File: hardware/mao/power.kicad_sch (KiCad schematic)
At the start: 36 parts, among them J101 USB-C, J102 BAT, Q101 AO3401A, U101 TPD2E2U06, U102 BQ24073RGTR, U103 MAX17048G+T10, U104 TPS63802DLAR, U105 TPS22919DCKR

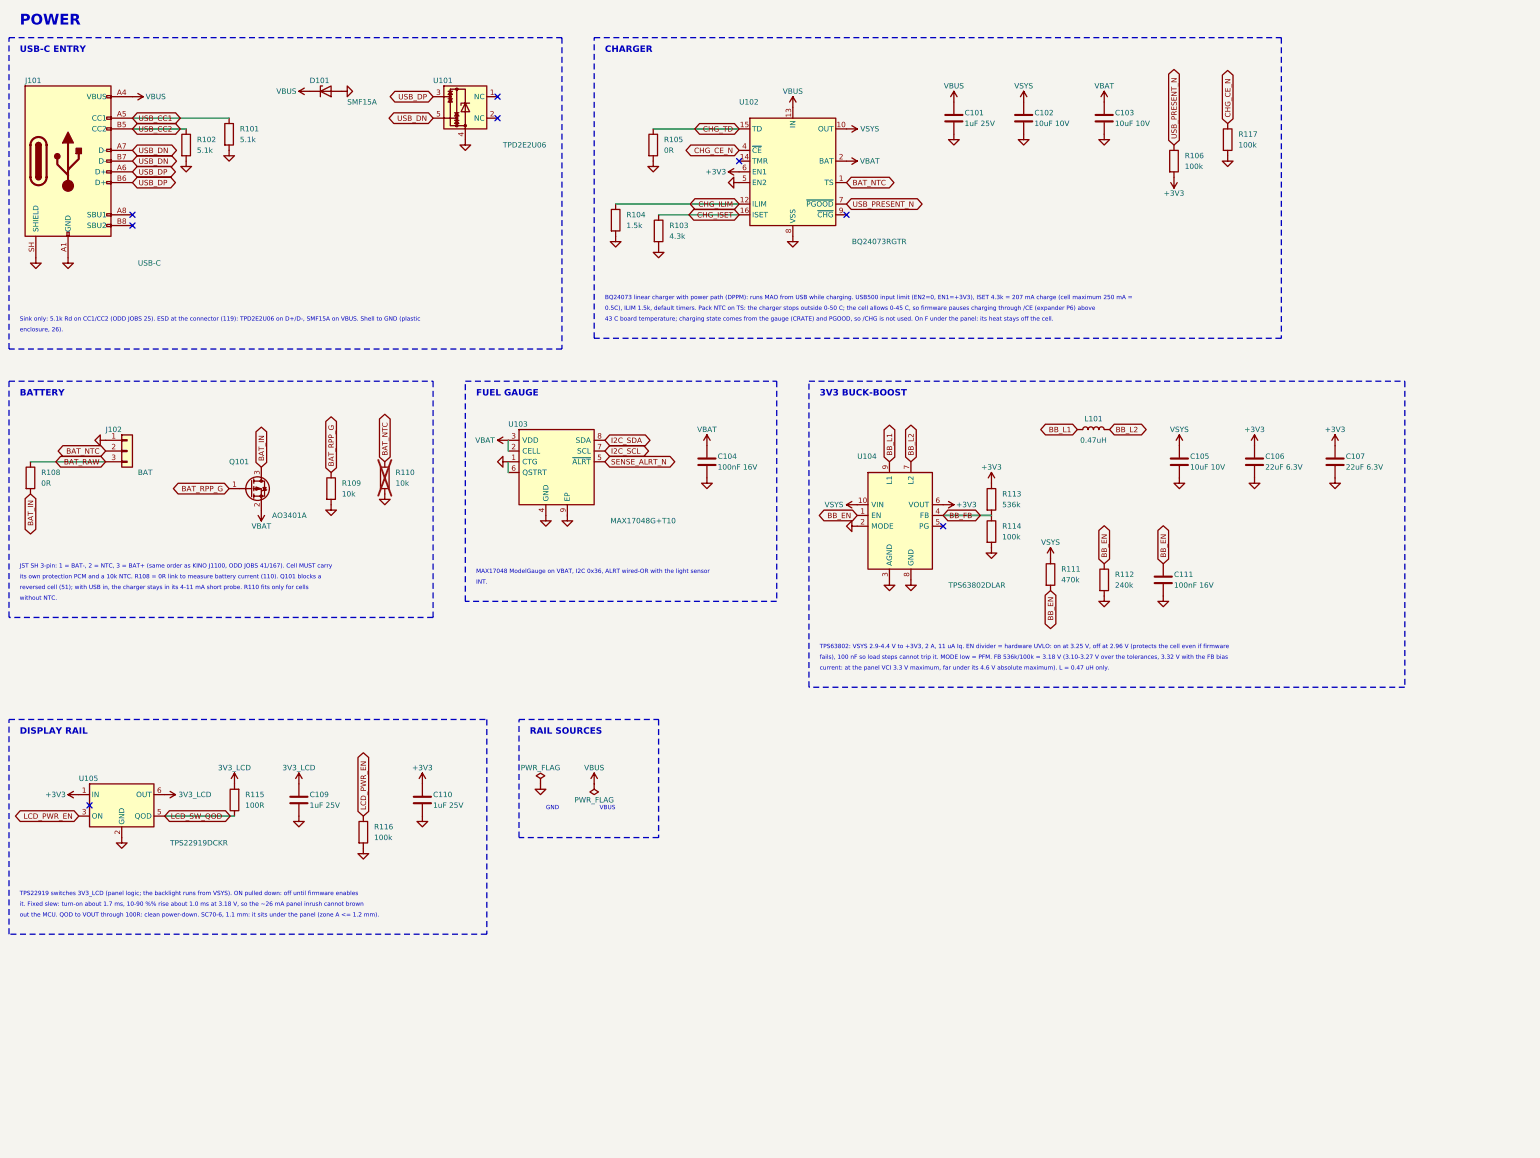
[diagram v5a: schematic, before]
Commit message: A1 capture: Gate C architecture on the A0 puck (schematic, ERC 0)
circuit.py now describes MAO_MAIN A1 (ERC 0 at all severities, 137 parts, 75 nets):
- ESP32-S3-MINI-1-N8 on RF_Module:ESP32-S2-MINI-1 (Gate C land audit); GPIO0 = BOOT pad only
  (10k + TP8), GPIO3/45/46 NC, 22R + DNP 10 pF on USB at the module, VBUS_SENSE 100k/150k.
- BQ25185 (ILIM/VSET 18k: 4.2 V / 500 mA; ISET 1.43k: 210 mA as A0; TS/MR to the NTC, DNP 10k,
  TSMR pad; /CE 100k pull-down; STAT1/2 10k to +3V3) replaces BQ24073.
- TPS62840 (VSET 102k = 3.2 V, SLVSEC6D table 1; 2.2 uH, CIN 4.7 uF, COUT 10 uF; MODE/STOP low,
  EN to VIN) replaces TPS63802 and its UVLO/FB dividers; LINK_REG 0R added, LINK_BAT kept.
- ICM-42670-P replaces LSM6DSOX on the same land (0x68, INT1 100k pull-up, INT2 not wired).
- DRV2605L VDD and pin 6 on +3V3; constant-current backlight sink (TLV9061 + DMG2302UK, 3.3R)
  replaces the AW9364; TPS22916C for the panel rail and the IR receiver rail.
- MAX98357A SD_MODE straight from GPIO9 (2.2k series dropped: +3V3 <= VSYS by topology).
- Removed: touch (4 zones, electrodes, springs), SPH0641, OPT3004, TCA6408A, board-ID divider.
- I2C pull-ups 4.7k; new fixture pads BL, AMP, TE, PRS, HLA, TSMR, CE, IO21, IO26.
- Battery connector stays JST SH: the Gate C JST PH side entry is 4.8 mm tall (KiCad STEP of the
  PH side-entry housing) against the 3.2 mm B-side zone over the cell; owner decision.
Parts kept from A0 keep their references; removed numbers are retired.
New footprint MAO:TI_DLC0008B_VSON-HR-8 (TI land example 4224310/A, from the Gate C generator);
A0-only custom footprints removed. Board name MAO_MAIN_A1; A0 board/outputs removed from this tree
(they stay on the A0 branch).

Co-Authored-By: Claude Opus 5.5 <noreply@anthropic.com>
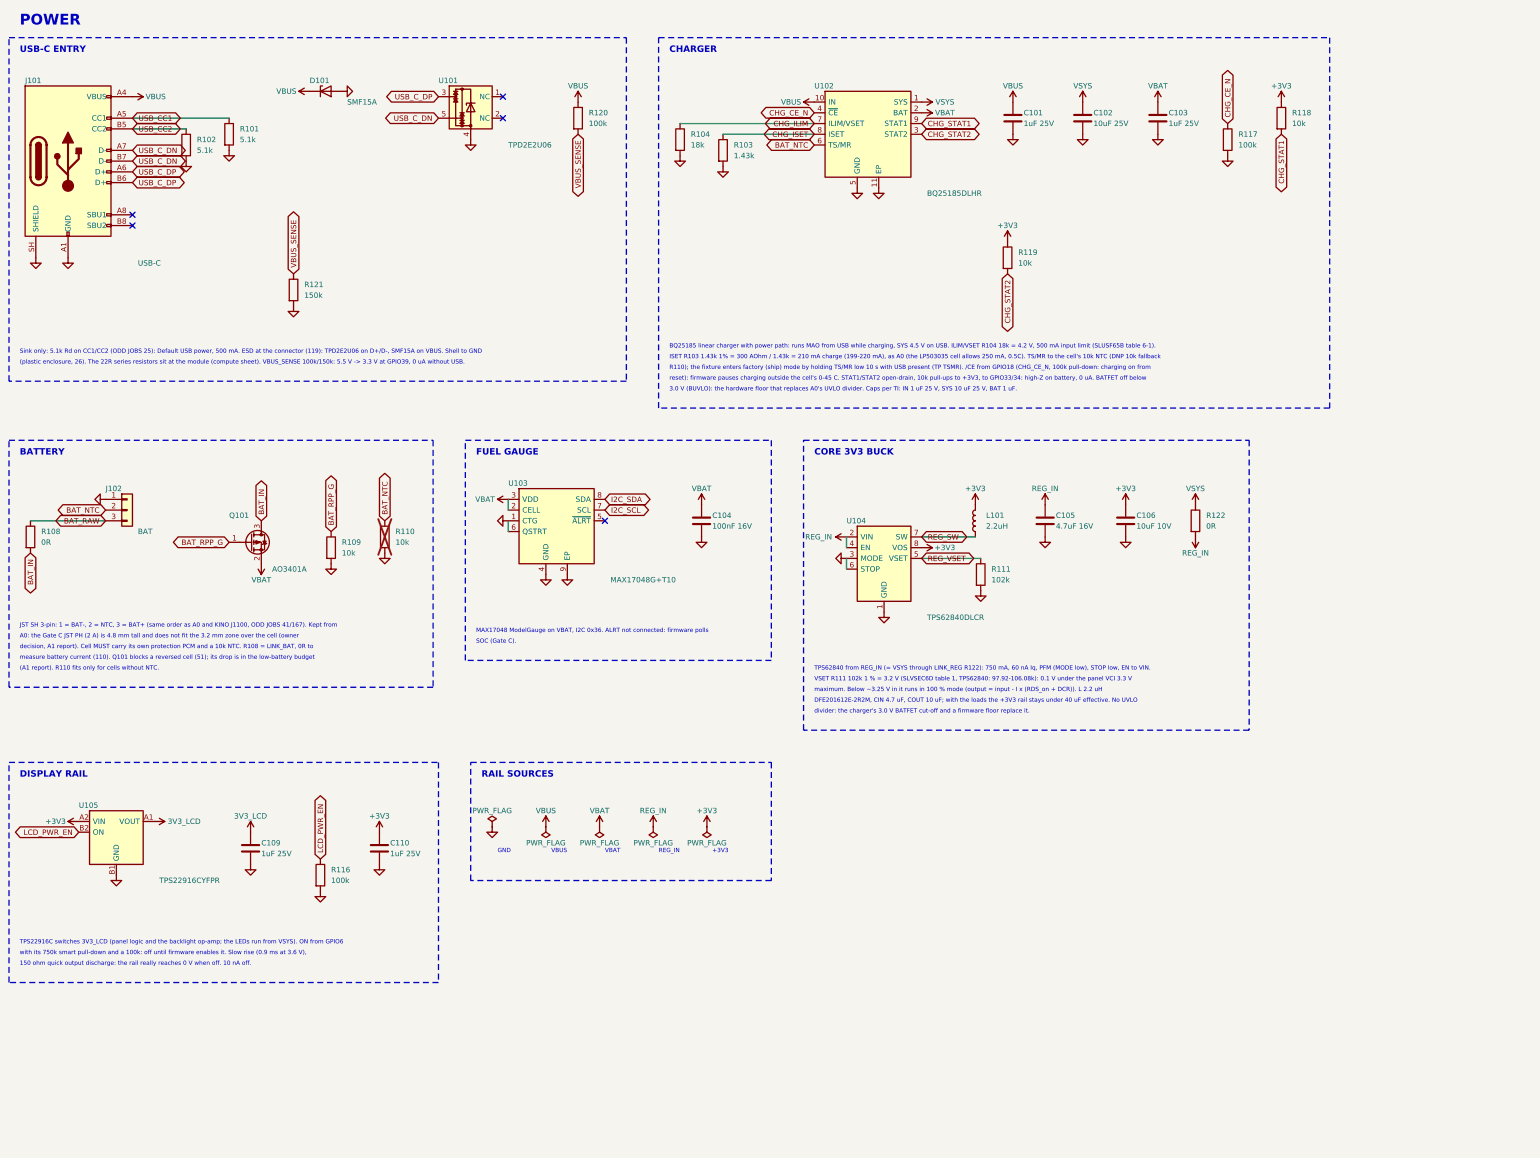
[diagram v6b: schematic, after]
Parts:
- removed C107: 22uF 6.3V, Capacitor_SMD:C_0603_1608Metric, symbol Device:C
- removed C111: 100nF 16V, Capacitor_SMD:C_0402_1005Metric, symbol Device:C
- removed R105: 0R, Resistor_SMD:R_0402_1005Metric, symbol Device:R
- removed R106, R114: 100k, Resistor_SMD:R_0402_1005Metric, symbol Device:R
- removed R112: 240k, Resistor_SMD:R_0402_1005Metric, symbol Device:R
- removed R113: 536k, Resistor_SMD:R_0402_1005Metric, symbol Device:R
- removed R115: 100R, Resistor_SMD:R_0402_1005Metric, symbol Device:R
- added R118, R119: 10k, Resistor_SMD:R_0402_1005Metric, symbol Device:R
- added R120: 100k, Resistor_SMD:R_0402_1005Metric, symbol Device:R
- added R121: 150k, Resistor_SMD:R_0402_1005Metric, symbol Device:R
- added R122: 0R, Resistor_SMD:R_0603_1608Metric, symbol Device:R
- C102: value 10uF 10V -> 10uF 25V; LCSC C19702 -> C96446; MPN CL10A106KP8NNNC -> CL10A106MA8NRNC
- C103: value 10uF 10V -> 1uF 25V; footprint Capacitor_SMD:C_0603_1608Metric -> Capacitor_SMD:C_0402_1005Metric; LCSC C19702 -> C52923; MPN CL10A106KP8NNNC -> CL05A105KA5NQNC
- C105: value 10uF 10V -> 4.7uF 16V; LCSC C19702 -> C19666; MPN CL10A106KP8NNNC -> CL10A475KO8NNNC
- C106: value 22uF 6.3V -> 10uF 10V; LCSC C59461 -> C19702; MPN CL10A226MQ8NRNC -> CL10A106KP8NNNC
- L101: value 0.47uH -> 2.2uH; LCSC C668312 -> C337893; MPN DFE201612E-R47M=P2 -> DFE201612E-2R2M=P2
- R103: value 4.3k -> 1.43k; LCSC C25899 -> C163483; MPN 0402WGF4301TCE -> RC0402FR-071K43L; Manufacturer UNI-ROYAL -> YAGEO
- R104: value 1.5k -> 18k; LCSC C25867 -> C25762; MPN 0402WGF1501TCE -> 0402WGF1802TCE
- R111: value 470k -> 102k; LCSC C25790 -> C2933066; MPN 0402WGF4703TCE -> FRC0402F1023TS; Manufacturer UNI-ROYAL -> FOJAN
- U102: value BQ24073RGTR -> BQ25185DLHR; footprint Package_DFN_QFN:VQFN-16-1EP_3x3mm_P0.5mm_EP1.68x1.68mm_ThermalVias -> Package_DFN_QFN:Texas_DLH0010A_WSON-10-1EP_2.2x2mm_P0.4mm_EP0.9x1.5mm; symbol Battery_Management:BQ24073RGT -> MAO:BQ25185; LCSC C15220 -> C19725033; MPN BQ24073RGTR -> BQ25185DLHR
- U104: value TPS63802DLAR -> TPS62840DLCR; footprint MAO:TI_DLA0010A_VSON-HR-10_2x3mm_P0.5mm -> MAO:TI_DLC0008B_VSON-HR-8_1.5x2mm_P0.5mm; symbol MAO:TPS63802 -> MAO:TPS62840; LCSC C2845237 -> C2071859; MPN TPS63802DLAR -> TPS62840DLCR
- U105: value TPS22919DCKR -> TPS22916CYFPR; footprint Package_TO_SOT_SMD:SOT-363_SC-70-6 -> Package_BGA:Texas_PicoStar_BGA-4_0.758x0.758mm_Layout2x2_P0.4mm; symbol Power_Management:TPS22919DCK -> MAO:TPS22916C; LCSC C2149796 -> C2680319; MPN TPS22919DCKR -> TPS22916CYFPR
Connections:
- net BB_EN is gone; now on net GND: R111.2, U104.1 (GND)
- net USB_PRESENT_N is gone; now on net CHG_ILIM: U102.7 (ILIM/VSET)
- net +3V3: now also L101.2, U104.8 (VOS), U105.A2 (VIN), R118.1, R119.1; no longer U102.6 (EN1), U104.6 (VOUT), U105.1 (IN)
- net 3V3_LCD: now also U105.A1 (VOUT); no longer U105.6 (OUT)
- net BAT_NTC: now also U102.6 (TS/MR); no longer U102.1 (TS)
- net CHG_ILIM: no longer U102.12 (ILIM)
- net CHG_ISET: now also U102.8 (ISET); no longer U102.16 (ISET)
- net GND: now also U102.11 (EP), U104.6 (STOP), U105.B1 (GND), R121.2; no longer U102.17 (VSS), U102.8 (VSS), U104.2 (MODE), U104.8 (GND), U105.2 (GND)
- net LCD_PWR_EN: now also U105.B2 (ON); no longer U105.3 (ON)
- net VBAT: no longer U102.3 (BAT)
- net VBUS: now also U102.10 (IN), R120.1; no longer U102.13 (IN)
- net VSYS: now also U102.1 (SYS), R122.1; no longer C105.1, R111.1, U102.10 (OUT), U102.11 (OUT), U104.10 (VIN)
- net REG_VSET: now reaches U104.5 (VSET)
- net REG_VSET: now also R111.1
- net CHG_STAT1: now reaches U102.9 (STAT1)
- net CHG_STAT1: now also R118.2
- net BB_FB renamed REG_IN
- net REG_IN: now also C105.1, U104.2 (VIN), R122.2
- net BB_L1 renamed REG_SW
- net REG_SW: now also U104.7 (SW); no longer U104.9 (L1)
- removed net BB_L2: L101.2, U104.7 (L2)
- removed net CHG_TD: U102.15 (TD)
- removed net LCD_SW_QOD: U105.5 (QOD)
- net SENSE_ALRT_N: no longer names the net of U103.5 (~{ALRT})
- net USB_DN renamed USB_C_DN
- net USB_DP renamed USB_C_DP
- new net CHG_STAT2: R119.2, U102.3 (STAT2)
- new net VBUS_SENSE: R120.2, R121.1
- no-connect marks 8 -> 5
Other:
- note added: "(A1 report). R110 fits only for cells without NTC."
- note added: "(plastic enclosure, 26). The 22R series resistors sit at the module (compute sheet). VBUS_SENSE 100k/150k: 5.5 V -> 3.3 V at GPIO39, 0 uA without USB."
- note added: "+3V3"
- note added: "150 ohm quick output discharge: the rail really reaches 0 V when off. 10 nA off."
- note added: "3.0 V (BUVLO): the hardware floor that replaces A0's UVLO divider. Caps per TI: IN 1 uF 25 V, SYS 10 uF 25 V, BAT 1 uF."
- note added: "A0: the Gate C JST PH (2 A) is 4.8 mm tall and does not fit the 3.2 mm zone over the cell (owner"
- note added: "BQ25185 linear charger with power path: runs MAO from USB while charging, SYS 4.5 V on USB. ILIM/VSET R104 18k = 4.2 V, 500 mA input limit (SLUSF65B table 6-1)."
- note added: "CORE 3V3 BUCK"
- note added: "DFE201612E-2R2M, CIN 4.7 uF, COUT 10 uF; with the loads the +3V3 rail stays under 40 uF effective. No UVLO"
- note added: "ISET R103 1.43k 1% = 300 AOhm / 1.43k = 210 mA charge (199-220 mA), as A0 (the LP503035 cell allows 250 mA, 0.5C). TS/MR to the cell's 10k NTC (DNP 10k fallback"
- note added: "JST SH 3-pin: 1 = BAT-, 2 = NTC, 3 = BAT+ (same order as A0 and KINO J1100, ODD JOBS 41/167). Kept from"
- note added: "MAX17048 ModelGauge on VBAT, I2C 0x36. ALRT not connected: firmware polls"
- note added: "R110); the fixture enters factory (ship) mode by holding TS/MR low 10 s with USB present (TP TSMR). /CE from GPIO18 (CHG_CE_N, 100k pull-down: charging on from"
- note added: "REG_IN"
- note added: "SOC (Gate C)."
- note added: "Sink only: 5.1k Rd on CC1/CC2 (ODD JOBS 25): Default USB power, 500 mA. ESD at the connector (119): TPD2E2U06 on D+/D-, SMF15A on VBUS. Shell to GND"
- note added: "TPS22916C switches 3V3_LCD (panel logic and the backlight op-amp; the LEDs run from VSYS). ON from GPIO6"
- note added: "TPS62840 from REG_IN (= VSYS through LINK_REG R122): 750 mA, 60 nA Iq, PFM (MODE low), STOP low, EN to VIN."
- note added: "VBAT"
- note added: "VSET R111 102k 1 % = 3.2 V (SLVSEC6D table 1, TPS62840: 97.92-106.08k): 0.1 V under the panel VCI 3.3 V"
- note added: "decision, A1 report). Cell MUST carry its own protection PCM and a 10k NTC. R108 = LINK_BAT, 0R to"
- note added: "divider: the charger's 3.0 V BATFET cut-off and a firmware floor replace it."
- note added: "maximum. Below ~3.25 V in it runs in 100 % mode (output = input - I x (RDS_on + DCR)). L 2.2 uH"
- note added: "measure battery current (110). Q101 blocks a reversed cell (51); its drop is in the low-battery budget"
- note added: "reset): firmware pauses charging outside the cell's 0-45 C. STAT1/STAT2 open-drain, 10k pull-ups to +3V3, to GPIO33/34: high-Z on battery, 0 uA. BATFET off below"
- note added: "with its 750k smart pull-down and a 100k: off until firmware enables it. Slow rise (0.9 ms at 3.6 V),"
- note removed: "0.5C), ILIM 1.5k, default timers. Pack NTC on TS: the charger stops outside 0-50 C; the cell allows 0-45 C, so firmware pauses charging through /CE (expander P6) above"
- note removed: "3V3 BUCK-BOOST"
- note removed: "43 C board temperature; charging state comes from the gauge (CRATE) and PGOOD, so /CHG is not used. On F under the panel: its heat stays off the cell."
- note removed: "BQ24073 linear charger with power path (DPPM): runs MAO from USB while charging. USB500 input limit (EN2=0, EN1=+3V3), ISET 4.3k = 207 mA charge (cell maximum 250 mA ="
- note removed: "INT."
- note removed: "JST SH 3-pin: 1 = BAT-, 2 = NTC, 3 = BAT+ (same order as KINO J1100, ODD JOBS 41/167). Cell MUST carry"
- note removed: "MAX17048 ModelGauge on VBAT, I2C 0x36, ALRT wired-OR with the light sensor"
- note removed: "Sink only: 5.1k Rd on CC1/CC2 (ODD JOBS 25). ESD at the connector (119): TPD2E2U06 on D+/D-, SMF15A on VBUS. Shell to GND (plastic"
- note removed: "TPS22919 switches 3V3_LCD (panel logic; the backlight runs from VSYS). ON pulled down: off until firmware enables"
- note removed: "TPS63802: VSYS 2.9-4.4 V to +3V3, 2 A, 11 uA Iq. EN divider = hardware UVLO: on at 3.25 V, off at 2.96 V (protects the cell even if firmware"
- note removed: "current: at the panel VCI 3.3 V maximum, far under its 4.6 V absolute maximum). L = 0.47 uH only."
- note removed: "enclosure, 26)."
- note removed: "fails), 100 nF so load steps cannot trip it. MODE low = PFM. FB 536k/100k = 3.18 V (3.10-3.27 V over the tolerances, 3.32 V with the FB bias"
- note removed: "it. Fixed slew: turn-on about 1.7 ms, 10-90 %% rise about 1.0 ms at 3.18 V, so the ~26 mA panel inrush cannot brown"
- note removed: "its own protection PCM and a 10k NTC. R108 = 0R link to measure battery current (110). Q101 blocks a"
- note removed: "out the MCU. QOD to VOUT through 100R: clean power-down. SC70-6, 1.1 mm: it sits under the panel (zone A <= 1.2 mm)."
- note removed: "reversed cell (51); with USB in, the charger stays in its 4-11 mA short probe. R110 fits only for cells"
- note removed: "without NTC."
- title: MAO_MAIN A0 - Power -> MAO_MAIN A1 - Power
- moved on the sheet: C101, C102, C103, C104, C105, C106, C109, C110, J102, L101, Q101, R103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
